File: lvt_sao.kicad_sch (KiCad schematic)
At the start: 15 parts, among them Q1 MMBT3904, U1 DFR0299, U2 HC-SR501, U3 ESP8266-01{slash}ESP-01, X1 Badgelife_sao_connector_v169b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

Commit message: Cleaned up the board and added graphics
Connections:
- net GND: now also U1.10 (GND), U1.7 (GND)
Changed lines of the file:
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@@
     (pin "3")
+  )
+  (symbol (lib_id "power:GND") (at 161.29 148.59 0) (unit 1)
+    (in_bom yes) (on_board yes) (fields_autoplaced)
+    (property "Reference" "#PWR0110" (id 0) (at 161.29 154.94 0)
+      (effects (font (size 1.27 1.27)) hide)
+    )
+    (property "Value" "GND" (id 1) (at 163.83 149.8599 0)
+      (effects (font (size 1.27 1.27)) (justify left))
+    )
+    (property "Footprint" "" (id 2) (at 161.29 148.59 0)
+      (effects (font (size 1.27 1.27)) hide)
+    )
+    (property "Datasheet" "" (id 3) (at 161.29 148.59 0)
+      (effects (font (size 1.27 1.27)) hide)
+    )
+    (pin "1")
   )
   (symbol (lib_id "Device:R") (at 240.03 99.06 90) (unit 1)
@@
       (reference "#PWR0109") (unit 1) (value "GND") (footprint "")
     )
+    (path "/8c9c23dd-8802-4fc0-b46e-0ebd1c81c6c8"
+      (reference "#PWR0110") (unit 1) (value "GND") (footprint "")
+    )
     (path "/9b1a0ddc-2815-4f35-824b-9e81fbeabbd5"

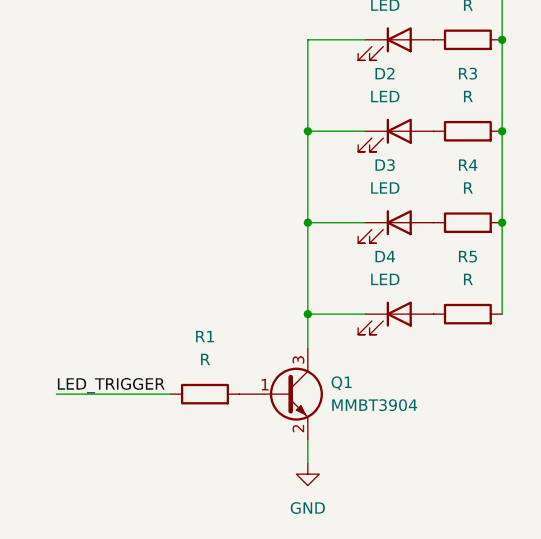
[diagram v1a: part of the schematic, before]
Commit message: Components arranged and traces added
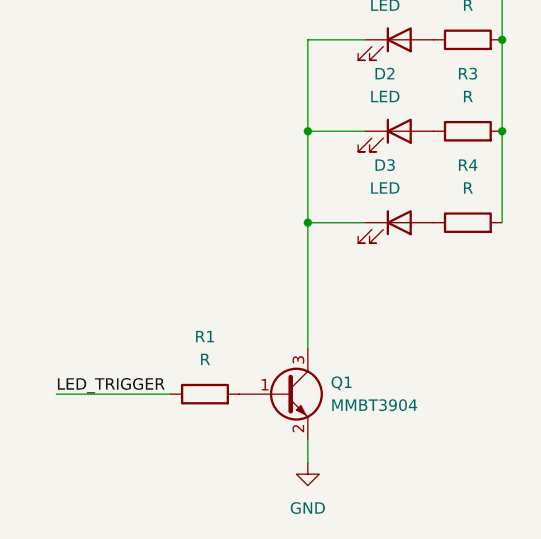
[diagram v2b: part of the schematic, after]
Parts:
- removed D4: LED, LED_SMD:LED_1210_3225Metric_Pad1.42x2.65mm_HandSolder, symbol Device:LED
- removed R5: R, Resistor_SMD:R_1210_3225Metric_Pad1.30x2.65mm_HandSolder, symbol Device:R
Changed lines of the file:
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@@
   (junction (at 243.84 109.22) (diameter 0) (color 0 0 0 0)
   )
-  (junction (at 222.25 129.54) (diameter 0) (color 0 0 0 0)
-  )
   (junction (at 243.84 99.06) (diameter 0) (color 0 0 0 0)
   )
-  (junction (at 243.84 119.38) (diameter 0) (color 0 0 0 0)
-  )
   (junction (at 222.25 109.22) (diameter 0) (color 0 0 0 0)
   )
@@
     (stroke (width 0) (type default) (color 0 0 0 0))
   )
-  (wire (pts (xy 243.84 119.38) (xy 243.84 129.54))
-    (stroke (width 0) (type default) (color 0 0 0 0))
-  )
   (wire (pts (xy 243.84 91.44) (xy 243.84 99.06))
     (stroke (width 0) (type default) (color 0 0 0 0))
@@
     (stroke (width 0) (type default) (color 0 0 0 0))
   )
-  (wire (pts (xy 228.6 129.54) (xy 222.25 129.54))
-    (stroke (width 0) (type default) (color 0 0 0 0))
-  )
   (wire (pts (xy 243.84 99.06) (xy 243.84 109.22))
     (stroke (width 0) (type default) (color 0 0 0 0))
@@
     (stroke (width 0) (type default) (color 0 0 0 0))
   )
-  (wire (pts (xy 222.25 119.38) (xy 222.25 129.54))
+  (wire (pts (xy 222.25 119.38) (xy 222.25 133.35))
     (stroke (width 0) (type default) (color 0 0 0 0))
   )
@@
   )
   (wire (pts (xy 222.25 146.05) (xy 222.25 143.51))
-    (stroke (width 0) (type default) (color 0 0 0 0))
-  )
-  (wire (pts (xy 222.25 129.54) (xy 222.25 133.35))
     (stroke (width 0) (type default) (color 0 0 0 0))
   )
@@
     (pin "2")
   )
-  (symbol (lib_id "Device:LED") (at 232.41 129.54 0) (unit 1)
-    (in_bom yes) (on_board yes) (fields_autoplaced)
-    (property "Reference" "D4" (id 0) (at 230.8225 123.19 0))
-    (property "Value" "LED" (id 1) (at 230.8225 125.73 0))
-    (property "Footprint" "LED_SMD:LED_1210_3225Metric_Pad1.42x2.65mm_HandSolder" (id 2) (at 232.41 129.54 0)
-      (effects (font (size 1.27 1.27)) hide)
-    )
-    (property "Datasheet" "~" (id 3) (at 232.41 129.54 0)
-      (effects (font (size 1.27 1.27)) hide)
-    )
-    (pin "1")
-    (pin "2")
-  )
   (symbol (lib_id "Transistor_BJT:MMBT3904") (at 219.71 138.43 0) (unit 1)
     (in_bom yes) (on_board yes) (fields_autoplaced)
@@
     )
     (property "Datasheet" "~" (id 3) (at 120.904 142.24 0)
-      (effects (font (size 1.27 1.27)) hide)
-    )
-    (pin "1")
-    (pin "2")
-  )
-  (symbol (lib_id "Device:R") (at 240.03 129.54 90) (unit 1)
-    (in_bom yes) (on_board yes) (fields_autoplaced)
-    (property "Reference" "R5" (id 0) (at 240.03 123.19 90))
-    (property "Value" "R" (id 1) (at 240.03 125.73 90))
-    (property "Footprint" "Resistor_SMD:R_1210_3225Metric_Pad1.30x2.65mm_HandSolder" (id 2) (at 240.03 131.318 90)
-      (effects (font (size 1.27 1.27)) hide)
-    )
-    (property "Datasheet" "~" (id 3) (at 240.03 129.54 0)
       (effects (font (size 1.27 1.27)) hide)
     )
@@
       (reference "D3") (unit 1) (value "LED") (footprint "LED_SMD:LED_1210_3225Metric_Pad1.42x2.65mm_HandSolder")
     )
-    (path "/b5066b55-0358-4550-9951-a29e4971d0f7"
-      (reference "D4") (unit 1) (value "LED") (footprint "LED_SMD:LED_1210_3225Metric_Pad1.42x2.65mm_HandSolder")
-    )
     (path "/c0b0c2cc-9206-479f-b334-046355cc2ab3"
       (reference "LS1") (unit 1) (value "Speaker") (footprint "Connector_PinHeader_2.54mm:PinHeader_1x02_P2.54mm_Vertical")
@@
       (reference "R4") (unit 1) (value "R") (footprint "Resistor_SMD:R_1210_3225Metric_Pad1.30x2.65mm_HandSolder")
     )
-    (path "/c2654a82-b7f7-41a5-8618-44853b8918b5"
-      (reference "R5") (unit 1) (value "R") (footprint "Resistor_SMD:R_1210_3225Metric_Pad1.30x2.65mm_HandSolder")
-    )
     (path "/58e17c7d-c31a-4295-bb6b-beeb534516db"

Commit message: final revision before ordering
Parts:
- removed Q1: MMBT3904, Package_TO_SOT_SMD:SOT-23, symbol Transistor_BJT:MMBT3904
- added J1: Conn_01x06_Male, Connector_PinHeader_2.54mm:PinHeader_1x06_P2.54mm_Vertical_SMD_Pin1Left, symbol Connector:Conn_01x06_Male
- added Q1: BC807, Package_TO_SOT_SMD:SOT-23, symbol Transistor_BJT:BC807
- added R5, R6, R7: R, Resistor_SMD:R_1210_3225Metric_Pad1.30x2.65mm_HandSolder, symbol Device:R
- LS1: footprint Connector_PinHeader_2.54mm:PinHeader_1x02_P2.54mm_Vertical -> Connector_PinHeader_2.54mm:PinHeader_1x02_P2.54mm_Vertical_SMD_Pin1Left
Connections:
- net ESP_UART_RX: now also J1.3 (Pin_3)
- net ESP_UART_TX: now also J1.4 (Pin_4)
- net GND: now also D1.1 (K), D2.1 (K), D3.1 (K)
- net LED_TRIGGER: now also U3.3 (IO0), J1.2 (Pin_2), R6.2, R7.1; no longer R1.1, U3.2 (IO2)
- net PIR_OUT: now also U3.2 (IO2); no longer U3.3 (IO0)
- net USB_D+: now also J1.5 (Pin_5)
- net USB_D-: now also J1.6 (Pin_6)
- net VCC: now also R1.2, Q1.2 (E), R5.2, R6.1; no longer R2.2, R3.2, R4.2
- net at U3.6 (EN): now also R1.1
- net RESET: now reaches U3.7 (~{RST})
- net RESET: now also J1.1 (Pin_1), R5.1
- new net: Q1.1 (B), R7.2
- new net: Q1.3 (C), R2.2, R3.2, R4.2
